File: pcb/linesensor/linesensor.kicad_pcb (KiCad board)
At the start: 2 copper layers, 21 x 12 mm, 2 parts, among them J1 Conn_01x03_Socket

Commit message: linesensor new
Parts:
- added R1: R, Resistor_THT:R_Axial_DIN0309_L9.0mm_D3.2mm_P12.70mm_Horizontal, F.Cu at (48.5, 40.4)
- added U1: TRCT5000, Library:CRT5000, F.Cu at (45.5, 34.0)
- R2: value 4,7 -> R; footprint Resistor_THT:R_Axial_DIN0207_L6.3mm_D2.5mm_P7.62mm_Horizontal -> Resistor_THT:R_Axial_DIN0309_L9.0mm_D3.2mm_P12.70mm_Horizontal
- moved R2 114.5 mm to (48.5, 27.4), turned to 180 degrees
- moved J1 111.1 mm to (32.6, 38.0), turned to 180 degrees
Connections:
- J1 pad 2: unconnected-(J1-Pin_2-Pad2) -> GND
- J1 pad 3: GND -> Net-(J1-Pin_3)
- R2 pad 1: GND -> Net-(R2-Pad1)
- R2 pad 2: Net-(R1-Pad2) -> Net-(J1-Pin_3)
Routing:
- net Net-(J1-Pin_1): track 0.00 -> 21.0 mm
- net Net-(J1-Pin_3): track 0.00 -> 6.78 mm
- net GND: track 6.11 -> 0.00 mm
- net Net-(R2-Pad1): track 0.00 -> 6.07 mm
- net Net-(U1A-Vdd): track 0.00 -> 3.47 mm
- added copper zone on F.Cu, net GND
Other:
- board size 21 x 12 mm -> 20.8 x 18.6 mm

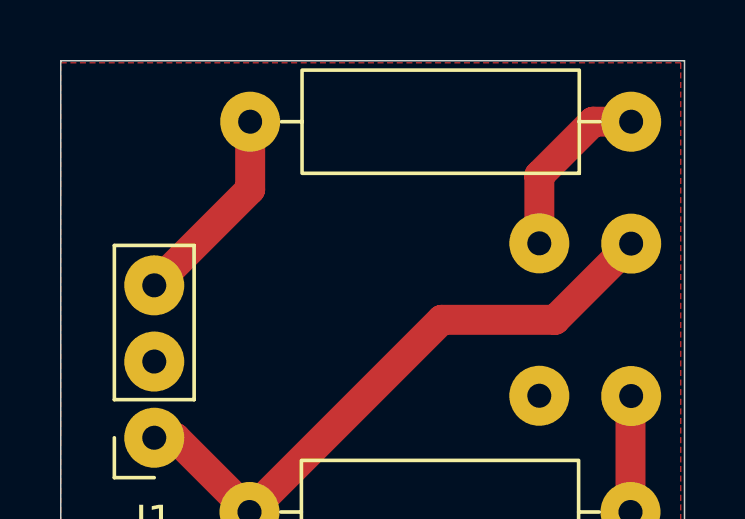
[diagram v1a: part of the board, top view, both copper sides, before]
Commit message: fixed line sensor PCB
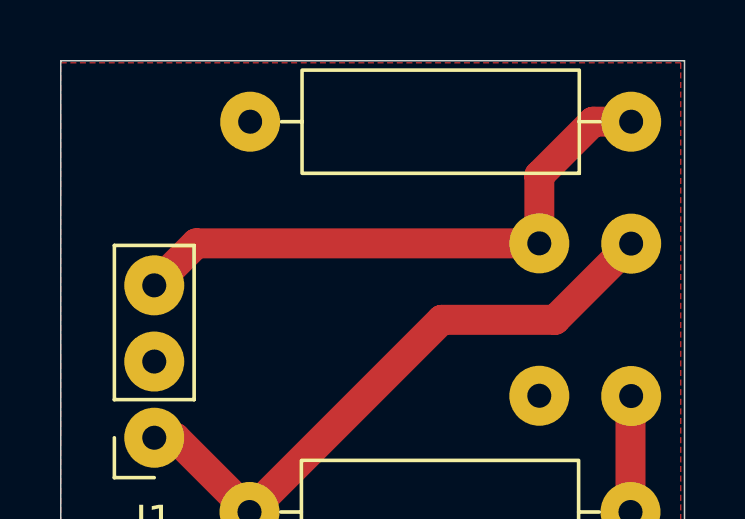
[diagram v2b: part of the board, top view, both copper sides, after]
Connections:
- R2 pad 1: Net-(R2-Pad1) -> Net-(J1-Pin_3)
- R2 pad 2: Net-(J1-Pin_3) -> GND
- U1 pad 3: Net-(R2-Pad1) -> Net-(J1-Pin_3)
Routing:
- net Net-(J1-Pin_3): track 6.78 -> 19.5 mm
- net Net-(R2-Pad1): track 6.07 -> 0.00 mm
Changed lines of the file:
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@@
 	(net 0 "")
 	(net 1 "Net-(J1-Pin_1)")
-	(net 2 "Net-(J1-Pin_3)")
-	(net 3 "GND")
-	(net 4 "Net-(U1A-Vdd)")
-	(net 5 "Net-(R2-Pad1)")
+	(net 2 "GND")
+	(net 3 "Net-(U1A-Vdd)")
+	(net 4 "Net-(J1-Pin_3)")
 	(footprint "Resistor_THT:R_Axial_DIN0309_L9.0mm_D3.2mm_P12.70mm_Horizontal"
 		(layer "F.Cu")
@@
 			(layers "*.Cu" "*.Mask")
 			(remove_unused_layers no)
-			(net 4 "Net-(U1A-Vdd)")
+			(net 3 "Net-(U1A-Vdd)")
 			(pintype "passive")
 		)
@@
 			(layers "*.Cu" "*.Mask")
 			(remove_unused_layers no)
-			(net 3 "GND")
+			(net 2 "GND")
 			(pinfunction "Pin_2")
 			(pintype "passive")
@@
 			(layers "*.Cu" "*.Mask")
 			(remove_unused_layers no)
-			(net 2 "Net-(J1-Pin_3)")
+			(net 4 "Net-(J1-Pin_3)")
 			(pinfunction "Pin_3")
 			(pintype "passive")
@@
 			(layers "*.Cu" "*.Mask")
 			(remove_unused_layers no)
-			(net 5 "Net-(R2-Pad1)")
+			(net 4 "Net-(J1-Pin_3)")
 			(pintype "passive")
 		)
@@
 			(layers "*.Cu" "*.Mask")
 			(remove_unused_layers no)
-			(net 2 "Net-(J1-Pin_3)")
+			(net 2 "GND")
 			(pintype "passive")
 		)
@@
 			(layers "*.Cu" "*.Mask")
 			(remove_unused_layers no)
-			(net 4 "Net-(U1A-Vdd)")
+			(net 3 "Net-(U1A-Vdd)")
 			(pinfunction "Vdd")
 			(pintype "power_in")
@@
 			(layers "*.Cu" "*.Mask")
 			(remove_unused_layers no)
-			(net 5 "Net-(R2-Pad1)")
+			(net 4 "Net-(J1-Pin_3)")
 			(pintype "input")
 		)
@@
 			(layers "*.Cu" "*.Mask")
 			(remove_unused_layers no)
-			(net 3 "GND")
+			(net 2 "GND")
 			(pinfunction "Vss")
 			(pintype "power_in")
@@
 	)
 	(segment
-		(start 35.814 29.689407)
-		(end 32.616942 32.886465)
-		(width 1)
-		(layer "F.Cu")
-		(net 2)
-	)
-	(segment
-		(start 35.814 27.432)
-		(end 35.814 29.689407)
-		(width 1)
-		(layer "F.Cu")
-		(net 2)
-	)
-	(segment
 		(start 48.491942 40.441465)
 		(end 48.491942 37.071942)
 		(width 1)
 		(layer "F.Cu")
-		(net 4)
+		(net 3)
 	)
 	(segment
@@
 		(width 1)
 		(layer "F.Cu")
-		(net 4)
+		(net 3)
 	)
 	(segment
@@
 		(width 1)
 		(layer "F.Cu")
-		(net 5)
+		(net 4)
 	)
 	(segment
@@
 		(width 1)
 		(layer "F.Cu")
-		(net 5)
+		(net 4)
 	)
 	(segment
@@
 		(width 1)
 		(layer "F.Cu")
-		(net 5)
+		(net 4)
+	)
+	(segment
+		(start 34.016292 31.487115)
+		(end 45.45193 31.487115)
+		(width 1)
+		(layer "F.Cu")
+		(net 4)
+	)
+	(segment
+		(start 32.616942 32.886465)
+		(end 34.016292 31.487115)
+		(width 1)
+		(layer "F.Cu")
+		(net 4)
 	)
 	(zone
-		(net 3)
+		(net 2)
 		(net_name "GND")
 		(layer "F.Cu")

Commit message: init
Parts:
- moved R2 16.1 mm to (32.5, 26.2), turned to -90 degrees
- moved R1 14.6 mm to (45.5, 26.2), turned to -90 degrees
- moved J1 11.2 mm to (43.0, 42.1), turned to -90 degrees
- moved U1 7.96 mm to (39.1, 29.2), turned to -90 degrees
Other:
- board size 20.8 x 18.6 mm -> 18.6 x 20.8 mm
